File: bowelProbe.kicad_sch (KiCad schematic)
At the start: 126 parts, among them J1 Conn_01x01, J10 Conn_01x01, J11 Conn_02x03_Odd_Even, J12 Conn_01x01, J13 Conn_01x01, J14 Conn_01x01, J15 Conn_01x01, J16 Conn_01x01, J17 Conn_01x01, J18 Conn_01x01, J19 Conn_01x01, J2 Conn_01x01, J20 Conn_01x01, J21 Conn_01x01, J22 Conn_01x01, J23 Conn_01x01, J24 Conn_01x01, J25 Conn_01x01, J3 Conn_01x08, J4 Conn_01x08, J5 Conn_01x01, J6 Conn_01x01, J7 Conn_01x01, J8 Conn_01x01, J9 Conn_01x01, Q1 AO3407A, U1 LM319MX/NOPB, U10 TLV76050DBZR, U11 TL072ACDR, U12 Buffer, U2 LT8330, U3 ATmega328P, U4 AD9833BRMZ, U5 SN74LVC1G86DBVR, U6 OPA2134UA/2K5, U7 TL072ACDR, U8 MCP6002T-E/MC, U9 LM3480IM3-12/NOPB

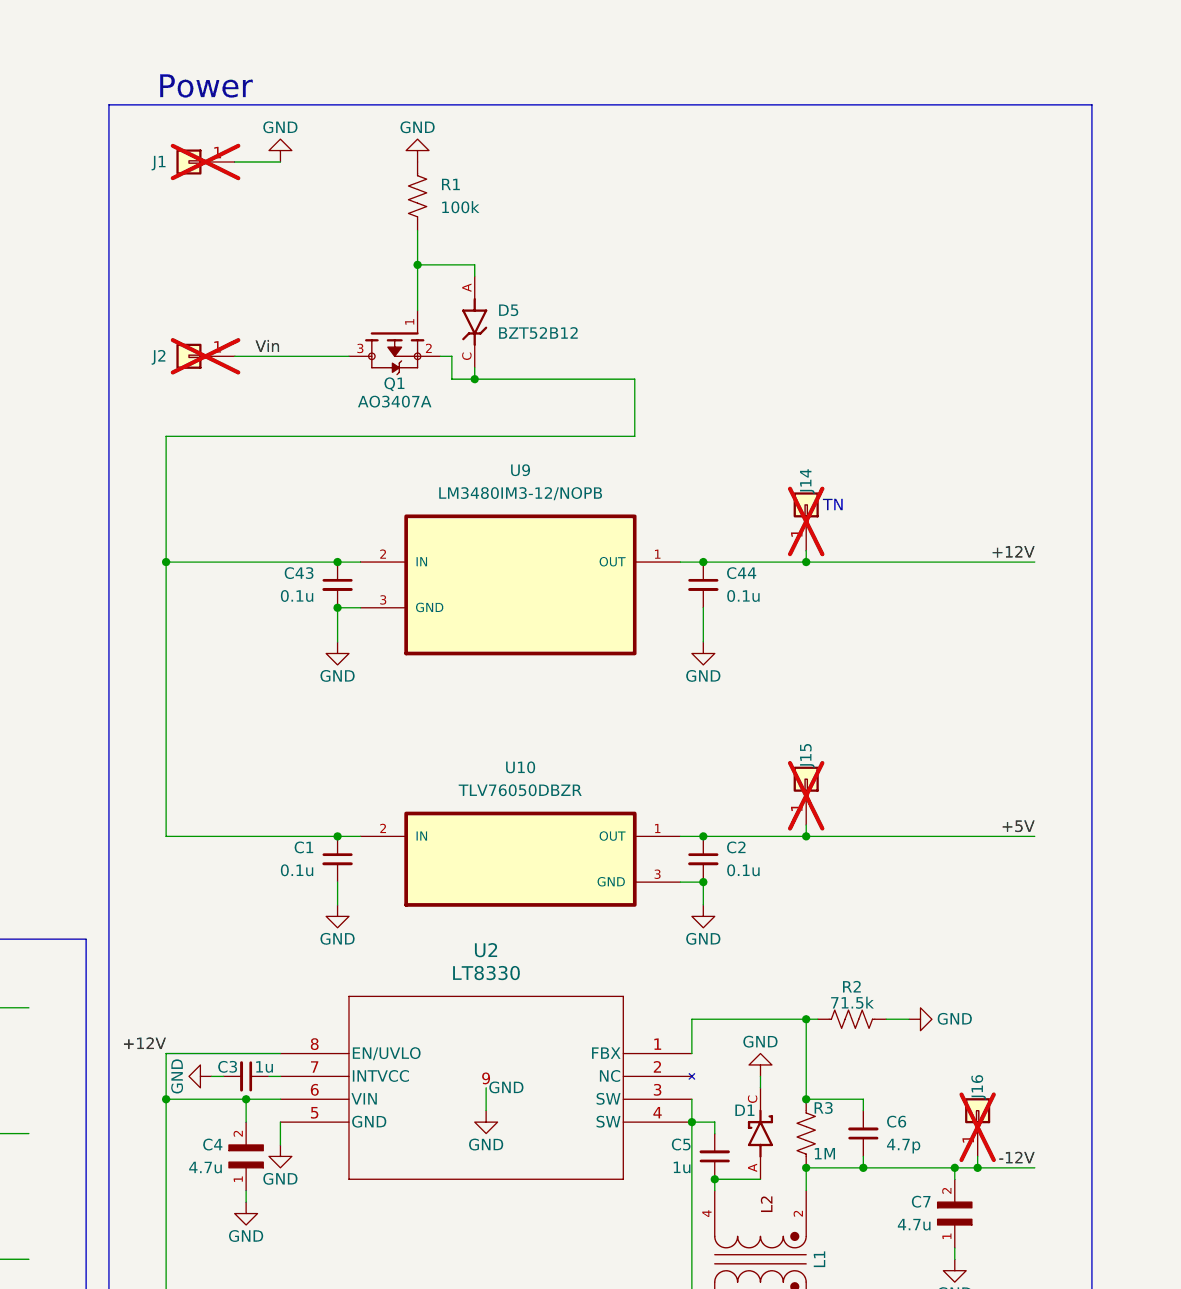
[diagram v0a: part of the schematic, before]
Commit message: Schematic Rough Draft Finished
Updated circuit for reverse polarity protection and fully updated BOM. Exported BOM to corresponding folder.
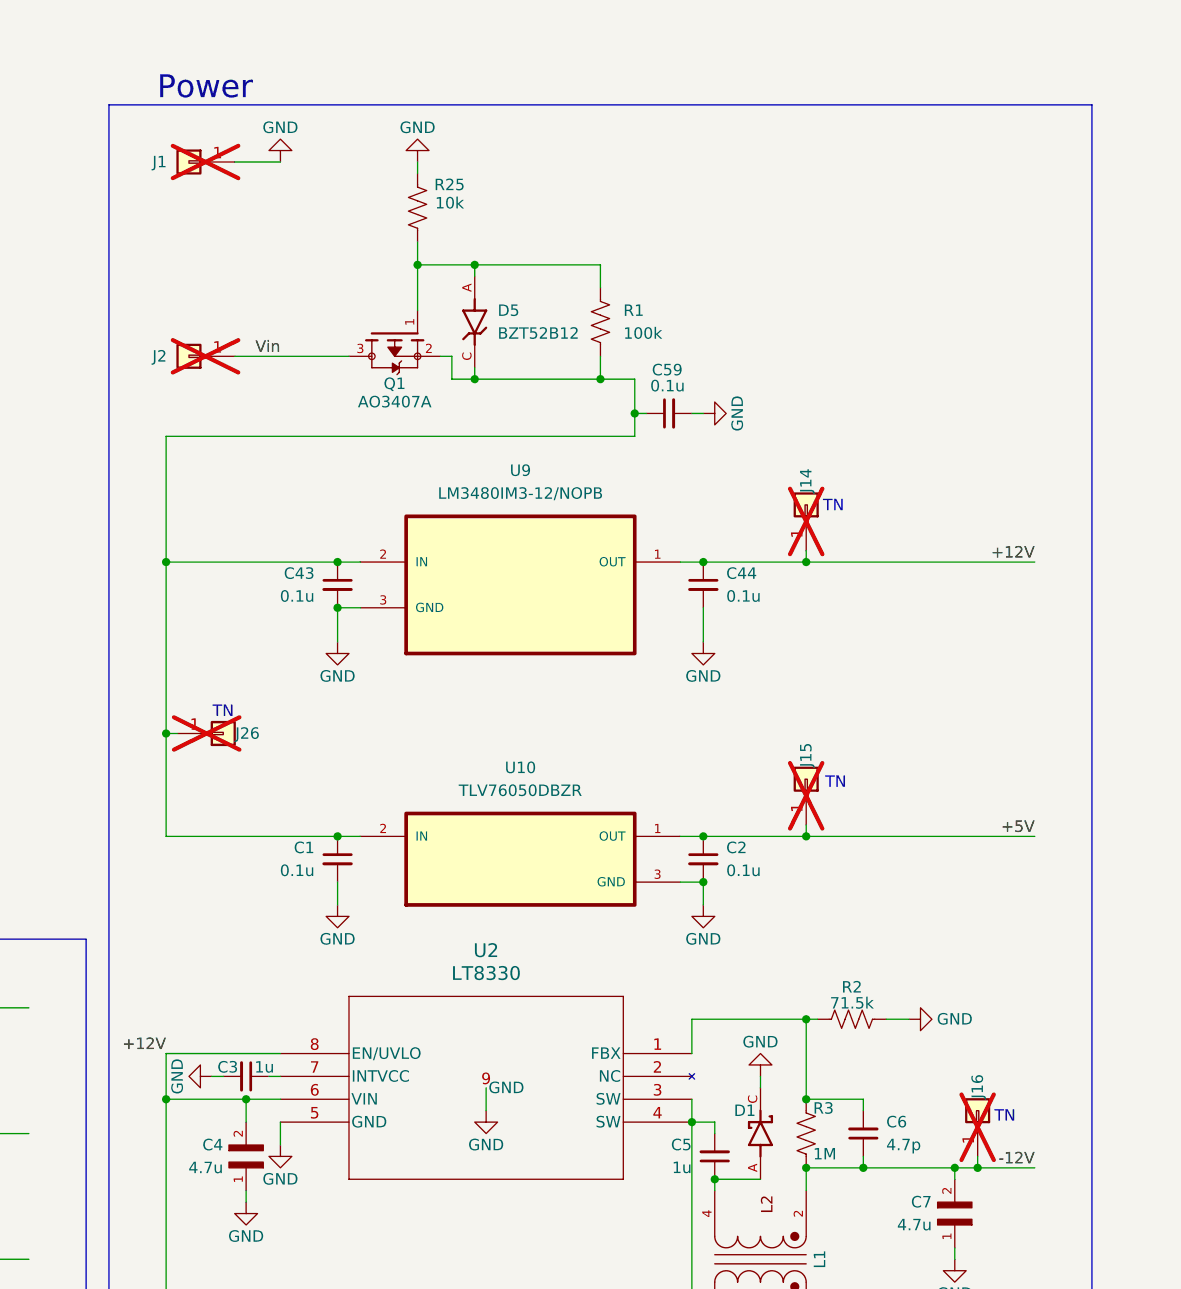
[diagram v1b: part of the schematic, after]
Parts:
- added C59: 0.1u, BowelProbe:Cap0.1uF, symbol Device:C_Small
- added J26: Conn_01x01, BowelProbe:CT3149-2, symbol Connector_Generic:Conn_01x01
- added R25: 10k, BowelProbe:Resistor10k, symbol Device:R_US
- D5: LCSC PN (none) -> C545349; Manufacturer (none) -> LGE
- Q1: LCSC PN (none) -> C15155; Manufacturer (none) -> Alpha & Omega Semicon
- R1: LCSC PN (none) -> C60491; Manufacturer (none) -> YAGEO
- U1: LCSC PN (none) -> C7941; Manufacturer (none) -> Texas Instruments
- U12: LCSC PN (none) -> C484731; Manufacturer (none) -> Texas Instruments
- U5: LCSC PN (none) -> C402161; Manufacturer (none) -> Texas Instruments
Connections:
- net GND: now also C59.2, R25.1; no longer R1.1
- net at D5.A, Q1.1: now also R1.1, R25.2; no longer R1.2
- net at C1.1, C43.1, D5.C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: now also R1.2, C59.1, J26.1 (Pin_1)
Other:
- moved on the sheet: R1

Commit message: BOM Revision
Revised BOM for in stock JLCPCB parts.
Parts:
- C30: LCSC PN C2168449 -> C513667; Manufacturer KEMET -> YAGEO
- D1: LCSC PN C406049 -> C27636122; Manufacturer Nexperia -> DOWO
- R14, R21, R24: LCSC PN C137314 -> C137155
- R15: LCSC PN C137372 -> C137188
- R2: LCSC PN C276313 -> C228984
- U2: LCSC PN C673746 -> C673743
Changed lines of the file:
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@@
 		(polyline
 			(pts
-				(xy 327.66 133.6675) (xy 495.3 133.0325) (xy 495.3 36.195) (xy 327.66 36.83)
+				(xy 13.97 166.37) (xy 57.15 166.37) (xy 57.15 147.32) (xy 138.43 147.32) (xy 138.43 13.97) (xy 13.97 13.97)
 			)
 			(stroke
 				(width 0)
 				(type solid)
-				(color 255 255 0 0.1)
+				(color 0 0 255 0.1)
 			)
 			(fill
 				(type color)
-				(color 255 255 0 0.1)
+				(color 0 0 255 0.1)
 			)
 		)
@@
 		(polyline
 			(pts
-				(xy 237.49 406.4) (xy 237.49 257.81) (xy 125.73 257.81) (xy 125.73 350.52) (xy 13.97 350.52) (xy 13.97 406.4)
+				(xy 327.66 133.6675) (xy 495.3 133.0325) (xy 495.3 36.195) (xy 327.66 36.83)
 			)
 			(stroke
 				(width 0)
 				(type solid)
-				(color 255 0 0 0.1)
+				(color 255 255 0 0.1)
 			)
 			(fill
 				(type color)
-				(color 255 0 0 0.1)
+				(color 255 255 0 0.1)
 			)
 		)
@@
 		(polyline
 			(pts
-				(xy 13.97 166.37) (xy 57.15 166.37) (xy 57.15 147.32) (xy 138.43 147.32) (xy 138.43 13.97) (xy 13.97 13.97)
+				(xy 237.49 406.4) (xy 237.49 257.81) (xy 125.73 257.81) (xy 125.73 350.52) (xy 13.97 350.52) (xy 13.97 406.4)
 			)
 			(stroke
 				(width 0)
 				(type solid)
-				(color 0 0 255 0.1)
+				(color 255 0 0 0.1)
 			)
 			(fill
 				(type color)
-				(color 0 0 255 0.1)
+				(color 255 0 0 0.1)
 			)
 		)
@@
 			)
 		)
-		(property "Description" "-55℃~+155℃ 200V 250mW 30kΩ Thick Film Resistor ±1% ±100ppm/℃ 1206 Chip Resistor - Surface Mount ROHS"
+		(property "Description" "-55℃~+155℃ 200V 250mW 30kΩ Thick Film Resistor ±100ppm/℃ ±5% 1206 Chip Resistor - Surface Mount ROHS"
 			(at 466.09 241.3 0)
 			(effects
@@
 			)
 		)
-		(property "LCSC PN" "C137314"
+		(property "LCSC PN" "C137155"
 			(at 466.09 241.3 0)
 			(effects
@@
 			)
 		)
-		(property "Description" "1 Independent 10A 1A 50uA@60V 60V 660mV@1A SOD-323F Schottky Diodes ROHS"
+		(property "Description" "1 Independent 100uA@60V 10A 1A 60V 700mV@1A SOD-323 Schottky Diodes ROHS"
 			(at 199.39 377.19 0)
 			(effects
@@
 			)
 		)
-		(property "Manufacturer" "Nexperia"
+		(property "Manufacturer" "DOWO"
 			(at 199.39 377.19 0)
 			(effects
@@
 			)
 		)
-		(property "LCSC PN" "C406049"
+		(property "LCSC PN" "C27636122"
 			(at 199.39 377.19 0)
 			(effects
@@
 			)
 		)
-		(property "Description" "-40℃~+125℃@(TJ) 1 1A 2MHz 3V~40V 6uA Adjustable Boost Boost、SEPIC、Inverting Built-in DFN-8(2x3) DC-DC Converters ROHS"
+		(property "Description" "-40℃~+150℃@(TJ) 1 1A 2MHz 3V~40V 6uA Adjustable Boost Boost、SEPIC、Inverting Built-in DFN-8(2x3) DC-DC Converters ROHS"
 			(at 191.77 367.03 0)
 			(effects
@@
 			)
 		)
-		(property "LCSC PN" "C673746"
+		(property "LCSC PN" "C673743"
 			(at 191.77 367.03 0)
 			(effects
@@
 			)
 		)
-		(property "Description" "-55℃~+155℃ 200V 250mW 30kΩ Thick Film Resistor ±1% ±100ppm/℃ 1206 Chip Resistor - Surface Mount ROHS"
+		(property "Description" "-55℃~+155℃ 200V 250mW 30kΩ Thick Film Resistor ±100ppm/℃ ±5% 1206 Chip Resistor - Surface Mount ROHS"
 			(at 429.26 110.49 0)
 			(effects
@@
 			)
 		)
-		(property "LCSC PN" "C137314"
+		(property "LCSC PN" "C137155"
 			(at 429.26 110.49 0)
 			(effects
@@
 			)
 		)
-		(property "Description" "-55℃~+155℃ 1.8kΩ 200V 250mW Thick Film Resistor ±1% ±100ppm/℃ 1206 Chip Resistor - Surface Mount ROHS"
+		(property "Description" "-55℃~+155℃ 1.8kΩ 200V 250mW Thick Film Resistor ±100ppm/℃ ±5% 1206 Chip Resistor - Surface Mount ROHS"
 			(at 438.15 114.3 0)
 			(effects
@@
 			)
 		)
-		(property "LCSC PN" "C137372"
+		(property "LCSC PN" "C137188"
 			(at 438.15 114.3 0)
 			(effects
@@
 			)
 		)
-		(property "LCSC PN" "C276313"
+		(property "LCSC PN" "C228984"
 			(at 209.55 364.49 0)
 			(effects
@@
 			)
 		)
-		(property "Description" "-55℃~+155℃ 200V 250mW 30kΩ Thick Film Resistor ±1% ±100ppm/℃ 1206 Chip Resistor - Surface Mount ROHS"
+		(property "Description" "-55℃~+155℃ 200V 250mW 30kΩ Thick Film Resistor ±100ppm/℃ ±5% 1206 Chip Resistor - Surface Mount ROHS"
 			(at 476.25 241.3 0)
 			(effects
@@
 			)
 		)
-		(property "LCSC PN" "C137314"
+		(property "LCSC PN" "C137155"
 			(at 476.25 241.3 0)
 			(effects
@@
 			)
 		)
-		(property "Manufacturer" "KEMET"
+		(property "Manufacturer" "YAGEO"
 			(at 349.25 104.14 0)
 			(effects
@@
 			)
 		)
-		(property "LCSC PN" "C2168449"
+		(property "LCSC PN" "C513667"
 			(at 349.25 104.14 0)
 			(effects

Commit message: Layout Update
Schematic rechecked and passed check #2. Initial rough draft layout nearly complete; just need to add stitching capacitors. Silkscreen text sizes and thicknesses changed.
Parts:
- removed J19: Conn_01x01, BowelProbe:CT3149-2, symbol Connector_Generic:Conn_01x01
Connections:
- net VinReverse: now reaches C1.1, C43.1, C59.1, D5.C, J26.1 (Pin_1), Q1.2, R1.2, U10.2 (IN), U9.2 (IN)
- net D9: now reaches U3.13 (PB1)
- net D10: now reaches U3.14 (PB2)
- net Vbuffer: no longer names the net of U7.1 (1OUT), U7.2 (1IN-), U7.5 (2IN+)
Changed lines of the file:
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@@
 		)
 	)
-	(text "TN"
-		(exclude_from_sim no)
-		(at 312.42 197.358 0)
-		(effects
-			(font
-				(size 1.27 1.27)
-			)
-		)
-	)
 	(text "Pin 1 - D12   Pin 2 - Vcc\nPin 3 - D13   Pin 4 - D11\nPin 5 - D10   Pin 6 - GND"
 		(exclude_from_sim no)
@@
 	)
 	(junction
-		(at 312.42 185.42)
-		(diameter 0)
-		(color 0 0 0 0)
-	)
-	(junction
 		(at 417.83 109.22)
 		(diameter 0)
@@
 	)
 	(no_connect
-		(at 76.2 86.36)
-	)
-	(no_connect
 		(at 24.13 151.13)
 	)
@@
 	)
 	(no_connect
-		(at 78.74 86.36)
+		(at 104.14 58.42)
 	)
 	(no_connect
-		(at 104.14 58.42)
+		(at 76.2 92.71)
 	)
 	(no_connect
@@
 	)
 	(no_connect
+		(at 78.74 92.71)
+	)
+	(no_connect
 		(at 477.52 171.45)
 	)
@@
 	(wire
 		(pts
-			(xy 68.58 41.91) (xy 68.58 48.26)
+			(xy 68.58 39.37) (xy 68.58 48.26)
 		)
 		(stroke
@@
 	(wire
 		(pts
-			(xy 66.04 41.91) (xy 66.04 48.26)
+			(xy 66.04 39.37) (xy 66.04 48.26)
 		)
 		(stroke
@@
 	(wire
 		(pts
-			(xy 81.28 41.91) (xy 81.28 48.26)
+			(xy 81.28 39.37) (xy 81.28 48.26)
 		)
 		(stroke
@@
 	(wire
 		(pts
+			(xy 78.74 86.36) (xy 78.74 92.71)
+		)
+		(stroke
+			(width 0)
+			(type default)
+			(color 194 194 0 1)
+		)
+	)
+	(wire
+		(pts
 			(xy 99.06 129.54) (xy 109.22 129.54)
 		)
@@
 	(wire
 		(pts
-			(xy 100.33 76.2) (xy 102.87 76.2)
+			(xy 100.33 76.2) (xy 104.14 76.2)
 		)
 		(stroke
@@
 	(wire
 		(pts
-			(xy 298.45 185.42) (xy 312.42 185.42)
+			(xy 298.45 185.42) (xy 335.28 185.42)
 		)
 		(stroke
@@
 	(wire
 		(pts
-			(xy 71.12 41.91) (xy 71.12 48.26)
+			(xy 71.12 39.37) (xy 71.12 48.26)
 		)
 		(stroke
@@
 	(wire
 		(pts
-			(xy 312.42 185.42) (xy 335.28 185.42)
-		)
-		(stroke
-			(width 0)
-			(type default)
-		)
-	)
-	(wire
-		(pts
 			(xy 556.26 227.33) (xy 560.07 227.33)
 		)
@@
 	(wire
 		(pts
+			(xy 76.2 86.36) (xy 76.2 92.71)
+		)
+		(stroke
+			(width 0)
+			(type default)
+			(color 194 194 0 1)
+		)
+	)
+	(wire
+		(pts
 			(xy 74.93 67.31) (xy 74.93 69.85)
 		)
@@
 	(wire
 		(pts
+			(xy 478.79 76.2) (xy 488.95 76.2)
+		)
+		(stroke
+			(width 0)
+			(type default)
+		)
+	)
+	(wire
+		(pts
 			(xy 331.47 240.03) (xy 340.36 240.03)
 		)
@@
 	(wire
 		(pts
-			(xy 312.42 186.69) (xy 312.42 185.42)
-		)
-		(stroke
-			(width 0)
-			(type default)
-		)
-	)
-	(wire
-		(pts
 			(xy 466.09 97.79) (xy 466.09 101.6)
 		)
@@
 		)
 	)
+	(label "VinReverse"
+		(at 133.35 337.82 0)
+		(effects
+			(font
+				(size 1.27 1.27)
+			)
+			(justify left bottom)
+		)
+	)
 	(label "B"
 		(at 447.04 186.69 0)
@@
 		)
 	)
+	(label "D10"
+		(at 78.74 92.71 90)
+		(effects
+			(font
+				(size 1.27 1.27)
+			)
+			(justify left bottom)
+		)
+	)
 	(label "RX"
-		(at 71.12 41.91 270)
+		(at 71.12 39.37 270)
 		(effects
 			(font
@@
 		)
 	)
-	(label "Vamplified"
-		(at 488.95 76.2 180)
-		(effects
-			(font
-				(size 1.27 1.27)
-			)
-			(justify right bottom)
-		)
-	)
 	(label "Vsingen"
 		(at 412.75 71.12 180)
@@
 	)
 	(label "SCK"
-		(at 102.87 76.2 180)
+		(at 104.14 76.2 180)
 		(effects
 			(font
@@
 		)
 	)
-	(label "Vbuffer"
-		(at 302.26 185.42 0)
+	(label "Vamplified"
+		(at 478.79 76.2 0)
 		(effects
 			(font
@@
 	)
 	(label "TX"
-		(at 68.58 41.91 270)
+		(at 68.58 39.37 270)
 		(effects
 			(font
@@
 	)
 	(label "D2"
-		(at 66.04 41.91 270)
+		(at 66.04 39.37 270)
 		(effects
 			(font
@@
 		)
 	)
+	(label "D9"
+		(at 76.2 92.71 90)
+		(effects
+			(font
+				(size 1.27 1.27)
+			)
+			(justify left bottom)
+		)
+	)
 	(label "SCK"
 		(at 99.06 132.08 0)
@@
 	)
 	(label "A3"
-		(at 81.28 41.91 270)
+		(at 81.28 39.37 270)
 		(effects
 			(font
@@
 		(polyline
 			(pts
-				(xy 13.97 166.37) (xy 57.15 166.37) (xy 57.15 147.32) (xy 138.43 147.32) (xy 138.43 13.97) (xy 13.97 13.97)
+				(xy 237.49 406.4) (xy 237.49 257.81) (xy 125.73 257.81) (xy 125.73 350.52) (xy 13.97 350.52) (xy 13.97 406.4)
 			)
 			(stroke
 				(width 0)
 				(type solid)
-				(color 0 0 255 0.1)
+				(color 255 0 0 0.1)
 			)
 			(fill
 				(type color)
-				(color 0 0 255 0.1)
+				(color 255 0 0 0.1)
 			)
 		)
@@
 		(polyline
 			(pts
-				(xy 327.66 133.6675) (xy 495.3 133.0325) (xy 495.3 36.195) (xy 327.66 36.83)
+				(xy 13.97 166.37) (xy 57.15 166.37) (xy 57.15 147.32) (xy 138.43 147.32) (xy 138.43 13.97) (xy 13.97 13.97)
 			)
 			(stroke
 				(width 0)
 				(type solid)
-				(color 255 255 0 0.1)
+				(color 0 0 255 0.1)
 			)
 			(fill
 				(type color)
-				(color 255 255 0 0.1)
+				(color 0 0 255 0.1)
 			)
 		)
@@
 		(polyline
 			(pts
-				(xy 237.49 406.4) (xy 237.49 257.81) (xy 125.73 257.81) (xy 125.73 350.52) (xy 13.97 350.52) (xy 13.97 406.4)
+				(xy 327.66 133.6675) (xy 495.3 133.0325) (xy 495.3 36.195) (xy 327.66 36.83)
 			)
 			(stroke
 				(width 0)
 				(type solid)
-				(color 255 0 0 0.1)
+				(color 255 255 0 0.1)
 			)
 			(fill
 				(type color)
-				(color 255 0 0 0.1)
+				(color 255 255 0 0.1)
 			)
 		)
@@
 		)
 		(pin "14"
-			(alternate "nSS")
 		)
 		(pin "9"
@@
 					(unit 1)
 				)
-			)
-		)
-	)
-	(symbol
-		(lib_id "Connector_Generic:Conn_01x01")
-		(at 312.42 191.77 90)
-		(mirror x)
-		(unit 1)
-		(exclude_from_sim no)
-		(in_bom no)
-		(on_board yes)
-		(dnp yes)
-		(property "Reference" "J19"
-			(at 312.42 195.834 0)
-			(effects
-				(font
-					(size 1.27 1.27)
-				)
-				(justify right)
-			)
-		)
-		(property "Value" "Conn_01x01"
-			(at 314.96 190.5001 90)
-			(effects
-				(font
-					(size 1.27 1.27)
-				)
-				(justify right)
-				(hide yes)
-			)
-		)
-		(property "Footprint" "BowelProbe:CT3149-2"
-			(at 312.42 191.77 0)
-			(effects
-				(font
-					(size 1.27 1.27)
-				)
-				(hide yes)
-			)
-		)
-		(property "Datasheet" "~"
-			(at 312.42 191.77 0)
-			(effects
-				(font
-					(size 1.27 1.27)
-				)
-				(hide yes)
-			)
-		)
-		(property "Description" "01x01 hole to fit wire"
-			(at 312.42 191.77 0)
-			(effects
-				(font
-					(size 1.27 1.27)
-				)
-				(hide yes)
-			)
-		)
-		(property "Order" "https://www.digikey.com/en/products/detail/cal-test-electronics/CT3149-2/5114523?gclsrc=aw.ds&gad_source=1&gad_campaignid=17336967819&gbraid=0AAAAADrbLlgHwoldOY3BTWvIRXP-Ifk7O&gclid=Cj0KCQiAg63LBhDtARIsAJygHZ6--plL5JvhXOV0g7-njs8DvOH5W1-zYAgOYW2KRe7TUxWEWHSgDDMaAp6TEALw_wcB"
-			(at 312.42 191.77 90)
-			(effects
-				(font
-					(size 1.27 1.27)
-				)
-				(hide yes)
-			)
-		)
-		(property "Purchase-URL" ""
-			(at 312.42 191.77 0)
-			(effects
-				(font
-					(size 1.27 1.27)
-				)
-			)
-		)
-		(property "Sim.Device" ""
-			(at 312.42 191.77 0)
-			(effects
-				(font
-					(size 1.27 1.27)
-				)
-			)
-		)
-		(property "Sim.Pins" ""
-			(at 312.42 191.77 0)
-			(effects
-				(font
-					(size 1.27 1.27)
-				)
-			)
-		)
-		(property "Sim.Pin" ""
-			(at 312.42 191.77 0)
-			(effects
-				(font
-					(size 1.27 1.27)
-				)
-			)
-		)
-		(property "Manufacturer Product Number" ""
-			(at 312.42 191.77 0)
-			(effects
-				(font
-					(size 1.27 1.27)
-				)
-			)
-		)
-		(property "LCSC PN" ""
-			(at 312.42 191.77 0)
-			(effects
-				(font
-					(size 1.27 1.27)
-				)
-			)
-		)
-		(pin "1"
-		)
-		(instances
-			(project "bowelProbe"
-				(path "/b054b76f-bc06-48fe-994a-b07fc1433235"
-					(reference "J19")
-					(unit 1)
-				)

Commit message: Layout Rough Draft Done
Placed all components where needed. Exposed remaining I/O pins on ATMega for miscellaneous use. Expected vias and stitching caps added. More stitching caps and vias will be added as necessary throughout and after routing. Considering possibility of moving logo and extra pin placements. Layout review coming up soon.
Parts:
- added J19, J27, J28, J29, J30, J31, J32: Conn_01x01, BowelProbe:CT3149-0, symbol Connector_Generic:Conn_01x01
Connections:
- net A0 is gone; now on net nSS_Sin: U3.23 (PC0)
- net A1: now also J32.1 (Pin_1)
- net D10: now also J30.1 (Pin_1)
- net D5: now also J19.1 (Pin_1)
- net D6: now also J27.1 (Pin_1)
- net D7: now also J28.1 (Pin_1)
- net D9: now also J29.1 (Pin_1)
- net nSS_Sin: no longer U3.25 (PC2)
- new net A2: J31.1 (Pin_1), U3.25 (PC2)
- no-connect marks 16 -> 9
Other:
- moved on the sheet: C1, C10, C11, C12, C13, C14, C15, C16, C2, C23, C24, C25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

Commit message: Layout and Routing Finished
Layout rough draft checked and cleared, routing finished on all layers, stitching caps added and schematic updated accordingly. Awaiting final board check before clearing for manufacture.
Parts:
- removed C10, C12, C15, C16, C8, C9: 0.1u, BowelProbe:Cap0.1uF, symbol Device:C_Small
- added C14: 0.1u, BowelProbe:Cap0.1uF, symbol Device:C_Small
- J16: renamed from J11; LCSC PN C6148500 -> (none); Manufacturer Sullins Connector Solutions -> (none)
- renumbered C17 to C1, C1 to C10, C2 to C11, C11 to C12, C14 to C15, C3 to C16, C4 to C17, C5 to C18, C6 to C19, C18 to C2, C7 to C20, C23 to C21, C24 to C22, C25 to C23, C26 to C24, C27 to C25, C48 to C26, C47 to C27, C45 to C28, C46 to C29, C21 to C3, C19 to C4, C51 to C43, C52 to C44, C49 to C45, C50 to C46, C53 to C47, C54 to C48, C57 to C49, C22 to C5, C58 to C50, C55 to C51, C56 to C52, C20 to C6, C59 to C7, C43 to C8, C44 to C9, D5 to D1, D1 to D2, D2 to D3, D3 to D4, D4 to D5, J3 to J1, J31 to J10, J32 to J11, J10 to J12, J6 to J13, J9 to J14, J5 to J15, J1 to J17, J2 to J18, J14 to J19, J4 to J2, J26 to J20, J15 to J21, J16 to J22, J17 to J23, J18 to J24, J12 to J25, J13 to J26, J20 to J27, J21 to J28, J22 to J29, J7 to J3, J23 to J30, J24 to J31, J25 to J32, J19 to J4, J27 to J5, J28 to J6, J29 to J7, J30 to J8, J8 to J9, L2 to L1, L1 to L2, R6 to R1, R25 to R10, R1 to R11, R2 to R12, R3 to R13, R11 to R14, R12 to R15, R13 to R16, R14 to R17, R15 to R18, R16 to R19, R5 to R2, R17 to R20, R18 to R21, R19 to R22, R20 to R23, R21 to R24, R24 to R25, R4 to R3, R22 to R4, R23 to R5, R9 to R6, R10 to R9, U3 to U1, U1 to U10, U5 to U11, U9 to U2, U10 to U3, U2 to U4, U4 to U5, U11 to U6, U6 to U7, U7 to U8, U8 to U9
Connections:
- net +5V: now also C14.1
- net GND: now also J16.1 (Pin_1), C14.2; no longer J16.6 (Pin_6)
- net MISO: now also J16.5 (Pin_5); no longer J16.1 (Pin_1)
- net nReset: now also J16.6 (Pin_6); no longer J16.5 (Pin_5)
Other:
- note added: "Pin 1 - GND Pin 2 - Vcc Pin 3 - D13 Pin 4 - D11 Pin 5 - D12 Pin 6 - D10"
- note removed: "Pin 1 - D12 Pin 2 - Vcc Pin 3 - D13 Pin 4 - D11 Pin 5 - D10 Pin 6 - GND"
- moved on the sheet: C15
